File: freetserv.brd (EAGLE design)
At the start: 91.4 x 82.5 mm, 157 parts, among them IC1 MCP16311-E/MS, IC10 MAX3232ECPW, IC11 MAX3232ECPW, IC12 MAX3232ECPW, IC13 MAX3232ECPW, IC14 FT4232HL, IC15 MAX3232ECPW, IC16 MAX3232ECPW, IC17 MAX3232ECPW, IC18 MAX3232ECPW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

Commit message: wire up DAISY_OUT
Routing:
- net DX0_P: track 2.89 -> 37.9 mm
- net DX0_N: track 2.89 -> 37.8 mm
- net +5V: track 98.0 -> 103.0 mm, vias 0 -> 1
- net D1_N: track 30.1 -> 32.3 mm
- net D1_P: track 30.5 -> 32.2 mm
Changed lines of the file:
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@@
 <contactref element="K1" pad="1"/>
 <contactref element="DAISY_OUT" pad="1"/>
-<wire x1="14.859" y1="81.026" x2="81.407" y2="81.026" width="0.4064" layer="16"/>
+<wire x1="14.859" y1="81.026" x2="16.891" y2="81.026" width="0.4064" layer="16"/>
+<wire x1="16.891" y1="81.026" x2="81.407" y2="81.026" width="0.4064" layer="16"/>
 <wire x1="81.407" y1="81.026" x2="81.407" y2="72.771" width="0.4064" layer="16"/>
 <wire x1="14.859" y1="81.026" x2="10.668" y2="81.026" width="0.4064" layer="1"/>
@@
 <wire x1="9.525" y1="79.883" x2="9.525" y2="76.962" width="0.4064" layer="1"/>
 <wire x1="9.525" y1="76.962" x2="5.207" y2="72.644" width="0.4064" layer="1"/>
-<wire x1="9.525" y1="76.962" x2="9.525" y2="75.057" width="0.4064" layer="1"/>
-<wire x1="9.525" y1="75.057" x2="13.208" y2="71.374" width="0.4064" layer="1"/>
-<wire x1="13.208" y1="71.374" x2="14.419" y2="71.374" width="0.4064" layer="1"/>
 <wire x1="14.419" y1="71.374" x2="14.46" y2="71.415" width="0.4064" layer="1"/>
+<wire x1="14.419" y1="71.374" x2="13.462" y2="71.374" width="0.4064" layer="1"/>
+<wire x1="13.462" y1="71.374" x2="13.208" y2="71.628" width="0.4064" layer="1"/>
+<via x="13.208" y="71.628" extent="1-16" drill="0.3048"/>
+<wire x1="13.208" y1="71.628" x2="13.208" y2="74.041" width="0.4064" layer="16"/>
+<wire x1="13.208" y1="74.041" x2="13.716" y2="74.549" width="0.4064" layer="16"/>
+<wire x1="13.716" y1="74.549" x2="15.494" y2="74.549" width="0.4064" layer="16"/>
+<wire x1="15.494" y1="74.549" x2="16.891" y2="75.946" width="0.4064" layer="16"/>
+<wire x1="16.891" y1="75.946" x2="16.891" y2="81.026" width="0.4064" layer="16"/>
+<wire x1="14.46" y1="71.415" x2="14.46" y2="72.065" width="0" layer="19" extent="1-1"/>
+<wire x1="14.544" y1="69.215" x2="14.419" y2="71.374" width="0" layer="19" extent="1-1"/>
+<wire x1="14.544" y1="67.056" x2="14.544" y2="69.215" width="0" layer="19" extent="1-1"/>
 </signal>
 <signal name="N$3">
@@
 <wire x1="70.8725" y1="74.3712" x2="71.1225" y2="74.1212" width="0.1778" layer="1" curve="-90"/>
 <wire x1="71.1225" y1="74.1212" x2="71.1225" y2="73.503" width="0.1778" layer="1"/>
-<wire x1="71.1225" y1="73.503" x2="75.239" y2="69.3865" width="0.1778" layer="1" curve="90"/>
-<wire x1="75.239" y1="69.3865" x2="76.289" y2="69.3865" width="0.1778" layer="1"/>
+<wire x1="76.289" y1="69.3865" x2="71.5835" y2="69.3865" width="0.1778" layer="1"/>
+<wire x1="71.5835" y1="69.3865" x2="71.12" y2="69.85" width="0.1778" layer="1" curve="-90"/>
+<wire x1="71.12" y1="69.85" x2="71.12" y2="73.5005" width="0.1778" layer="1"/>
+<wire x1="71.12" y1="73.5005" x2="71.1225" y2="73.503" width="0.1778" layer="1" curve="-90"/>
 </signal>
 <signal name="D1_P" class="1">
@@
 <wire x1="51.094053125" y1="72.3138" x2="52.08856875" y2="72.3138" width="0.1778" layer="1"/>
 <wire x1="53.467" y1="72.3138" x2="66.370796875" y2="72.3138" width="0.1778" layer="1"/>
-<wire x1="76.289" y1="70.1865" x2="73.0225" y2="73.453" width="0.1778" layer="1" curve="-90"/>
-<wire x1="73.0225" y1="73.453" x2="73.0225" y2="73.503" width="0.1778" layer="1"/>
+<wire x1="73.0225" y1="70.6145" x2="73.0225" y2="73.503" width="0.1778" layer="1"/>
+<wire x1="73.0225" y1="70.6145" x2="73.279" y2="70.358" width="0.1778" layer="1" curve="90"/>
+<wire x1="73.279" y1="70.358" x2="76.1175" y2="70.358" width="0.1778" layer="1"/>
+<wire x1="76.1175" y1="70.358" x2="76.289" y2="70.1865" width="0.1778" layer="1" curve="-90"/>
 </signal>
 <signal name="DX0_N" class="1">
@@
 <wire x1="30.5625" y1="76.012290625" x2="30.5625" y2="75.603" width="0.1778" layer="1"/>
 <contactref element="DAISY_OUT" pad="3"/>
-<wire x1="5.207" y1="67.564" x2="30.5625" y2="75.603" width="0" layer="19" extent="1-1"/>
+<wire x1="30.5625" y1="75.603" x2="30.5625" y2="75.3935" width="0.1778" layer="1"/>
+<wire x1="30.5625" y1="75.3935" x2="30.226" y2="75.057" width="0.1778" layer="1" curve="-90"/>
+<wire x1="30.226" y1="75.057" x2="12.446" y2="75.057" width="0.1778" layer="1"/>
+<wire x1="12.446" y1="75.057" x2="11.938" y2="74.549" width="0.1778" layer="1" curve="90"/>
+<wire x1="11.938" y1="74.549" x2="11.938" y2="67.945" width="0.1778" layer="1"/>
+<wire x1="11.938" y1="67.945" x2="11.557" y2="67.564" width="0.1778" layer="1" curve="-90"/>
+<wire x1="11.557" y1="67.564" x2="10.730065625" y2="67.564" width="0.1778" layer="1"/>
+<wire x1="10.730065625" y1="67.564" x2="10.418915625" y2="67.87515" width="0.1778" layer="1" curve="-90"/>
+<wire x1="10.418915625" y1="67.87515" x2="10.107765625" y2="68.1863" width="0.1778" layer="1" curve="90"/>
+<wire x1="10.107765625" y1="68.1863" x2="9.985478125" y2="68.1863" width="0.1778" layer="1"/>
+<wire x1="9.985478125" y1="68.1863" x2="9.674328125" y2="67.87515" width="0.1778" layer="1" curve="90"/>
+<wire x1="9.674328125" y1="67.87515" x2="9.674328125" y2="67.25285" width="0.1778" layer="1"/>
+<wire x1="9.674328125" y1="67.25285" x2="9.363178125" y2="66.9417" width="0.1778" layer="1" curve="-90"/>
+<wire x1="9.363178125" y1="66.9417" x2="9.2408875" y2="66.9417" width="0.1778" layer="1"/>
+<wire x1="9.2408875" y1="66.9417" x2="8.9297375" y2="67.25285" width="0.1778" layer="1" curve="-90"/>
+<wire x1="8.9297375" y1="67.25285" x2="8.9297375" y2="67.87515" width="0.1778" layer="1"/>
+<wire x1="8.9297375" y1="67.87515" x2="8.6185875" y2="68.1863" width="0.1778" layer="1" curve="90"/>
+<wire x1="8.6185875" y1="68.1863" x2="8.4963" y2="68.1863" width="0.1778" layer="1"/>
+<wire x1="8.4963" y1="68.1863" x2="8.18515" y2="67.87515" width="0.1778" layer="1" curve="90"/>
+<wire x1="8.18515" y1="67.87515" x2="7.874" y2="67.564" width="0.1778" layer="1" curve="-90"/>
+<wire x1="7.874" y1="67.564" x2="5.207" y2="67.564" width="0.1778" layer="1"/>
 </signal>
 <signal name="DX0_P" class="1">
@@
 <wire x1="29.7625" y1="76.012290625" x2="29.7625" y2="75.603" width="0.1778" layer="1"/>
 <contactref element="DAISY_OUT" pad="2"/>
-<wire x1="5.207" y1="70.104" x2="29.7625" y2="75.603" width="0" layer="19" extent="1-1"/>
+<wire x1="12.357" y1="75.603" x2="29.7625" y2="75.603" width="0.1778" layer="1"/>
+<wire x1="12.357" y1="75.603" x2="11.43" y2="74.676" width="0.1778" layer="1" curve="90"/>
+<wire x1="11.43" y1="74.676" x2="11.43" y2="70.612" width="0.1778" layer="1"/>
+<wire x1="11.43" y1="70.612" x2="10.922" y2="70.104" width="0.1778" layer="1" curve="-90"/>
+<wire x1="10.922" y1="70.104" x2="10.914053125" y2="70.104" width="0.1778" layer="1"/>
+<wire x1="10.914053125" y1="70.104" x2="10.602903125" y2="69.79285" width="0.1778" layer="1" curve="90"/>
+<wire x1="10.602903125" y1="69.79285" x2="10.602903125" y2="69.620953125" width="0.1778" layer="1"/>
+<wire x1="10.602903125" y1="69.620953125" x2="10.291753125" y2="69.309803125" width="0.1778" layer="1" curve="-90"/>
+<wire x1="10.291753125" y1="69.309803125" x2="10.278103125" y2="69.309803125" width="0.1778" layer="1"/>
+<wire x1="10.278103125" y1="69.309803125" x2="9.966953125" y2="69.620953125" width="0.1778" layer="1" curve="-90"/>
+<wire x1="9.966953125" y1="69.620953125" x2="9.966953125" y2="70.587046875" width="0.1778" layer="1"/>
+<wire x1="9.966953125" y1="70.587046875" x2="9.655803125" y2="70.898196875" width="0.1778" layer="1" curve="90"/>
+<wire x1="9.655803125" y1="70.898196875" x2="9.642153125" y2="70.898196875" width="0.1778" layer="1"/>
+<wire x1="9.642153125" y1="70.898196875" x2="9.331003125" y2="70.587046875" width="0.1778" layer="1" curve="90"/>
+<wire x1="9.331003125" y1="70.587046875" x2="9.331003125" y2="69.620953125" width="0.1778" layer="1"/>
+<wire x1="9.331003125" y1="69.620953125" x2="9.019853125" y2="69.309803125" width="0.1778" layer="1" curve="-90"/>
+<wire x1="9.019853125" y1="69.309803125" x2="9.0062" y2="69.309803125" width="0.1778" layer="1"/>
+<wire x1="9.0062" y1="69.309803125" x2="8.69505" y2="69.620953125" width="0.1778" layer="1" curve="-90"/>
+<wire x1="8.69505" y1="69.620953125" x2="8.69505" y2="70.587046875" width="0.1778" layer="1"/>
+<wire x1="8.69505" y1="70.587046875" x2="8.3839" y2="70.898196875" width="0.1778" layer="1" curve="90"/>
+<wire x1="8.3839" y1="70.898196875" x2="8.37025" y2="70.898196875" width="0.1778" layer="1"/>
+<wire x1="8.37025" y1="70.898196875" x2="8.0591" y2="70.587046875" width="0.1778" layer="1" curve="90"/>
+<wire x1="8.0591" y1="70.587046875" x2="8.0591" y2="69.620953125" width="0.1778" layer="1"/>
+<wire x1="8.0591" y1="69.620953125" x2="7.74795" y2="69.309803125" width="0.1778" layer="1" curve="-90"/>
+<wire x1="7.74795" y1="69.309803125" x2="7.7343" y2="69.309803125" width="0.1778" layer="1"/>
+<wire x1="7.7343" y1="69.309803125" x2="7.42315" y2="69.620953125" width="0.1778" layer="1" curve="-90"/>
+<wire x1="7.42315" y1="69.620953125" x2="7.42315" y2="69.79285" width="0.1778" layer="1"/>
+<wire x1="7.42315" y1="69.79285" x2="7.112" y2="70.104" width="0.1778" layer="1" curve="90"/>
+<wire x1="7.112" y1="70.104" x2="5.207" y2="70.104" width="0.1778" layer="1"/>
 </signal>
 <signal name="D0_N" class="1">

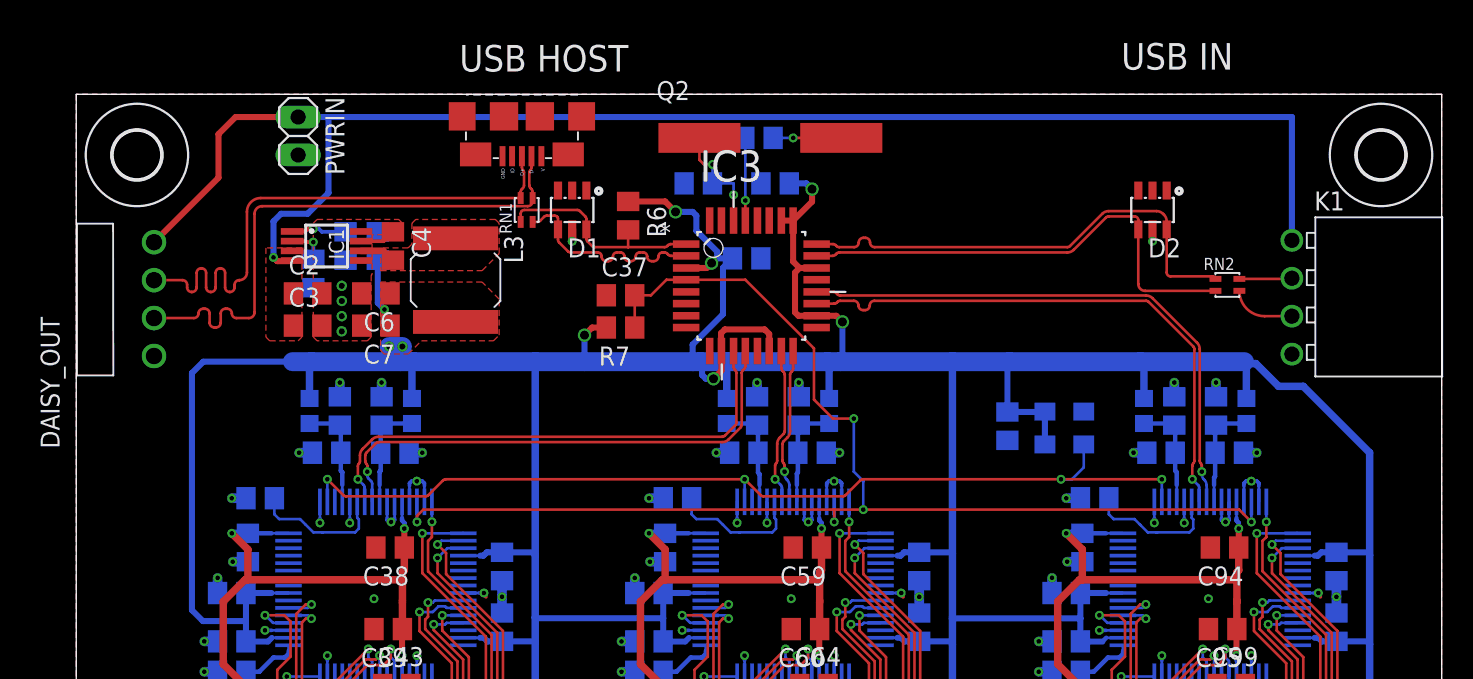
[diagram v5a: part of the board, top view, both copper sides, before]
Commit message: add tPlace documentation (port descriptions, version)
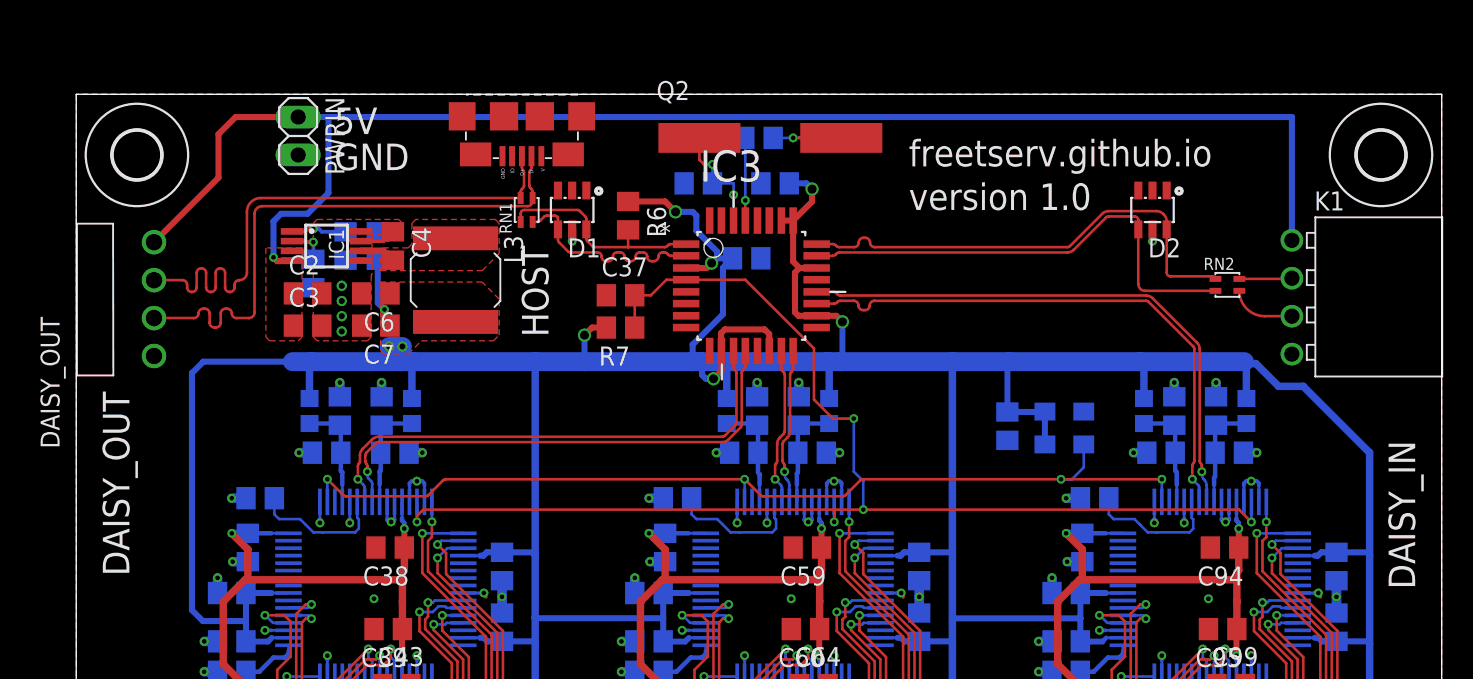
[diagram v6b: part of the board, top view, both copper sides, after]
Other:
- board text added: "5V"
- board text added: "DAISY_IN"
- board text added: "DAISY_OUT"
- board text added: "GND"
- board text added: "HOST"
- board text added: "freetserv.github.io"
- board text added: "version 1.0"
- board text removed: "USB HOST"
- board text removed: "USB IN"
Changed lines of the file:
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@@
 <wire x1="91.44" y1="82.55" x2="0" y2="82.55" width="0" layer="20"/>
 <wire x1="0" y1="82.55" x2="0" y2="0" width="0" layer="20"/>
-<text x="69.977" y="84.201" size="1.778" layer="21">USB IN</text>
-<text x="25.654" y="84.074" size="1.778" layer="21">USB HOST</text>
+<text x="31.623" y="66.294" size="1.778" layer="21" rot="R90">HOST</text>
+<text x="17.272" y="77.47" size="1.778" layer="21">GND</text>
+<text x="17.272" y="79.883" size="1.778" layer="21">5V</text>
+<text x="3.556" y="50.292" size="1.778" layer="21" rot="R90">DAISY_OUT</text>
+<text x="89.662" y="49.403" size="1.778" layer="21" rot="R90">DAISY_IN</text>
+<text x="55.753" y="77.724" size="1.778" layer="21">freetserv.github.io</text>
+<text x="55.753" y="74.803" size="1.778" layer="21">version 1.0</text>
 </plain>
 <attributes>
@@
 <wire x1="15.494" y1="74.549" x2="16.891" y2="75.946" width="0.4064" layer="16"/>
 <wire x1="16.891" y1="75.946" x2="16.891" y2="81.026" width="0.4064" layer="16"/>
-<wire x1="14.46" y1="71.415" x2="14.46" y2="72.065" width="0" layer="19" extent="1-1"/>
-<wire x1="14.544" y1="69.215" x2="14.419" y2="71.374" width="0" layer="19" extent="1-1"/>
-<wire x1="14.544" y1="67.056" x2="14.544" y2="69.215" width="0" layer="19" extent="1-1"/>
 </signal>
 <signal name="N$3">

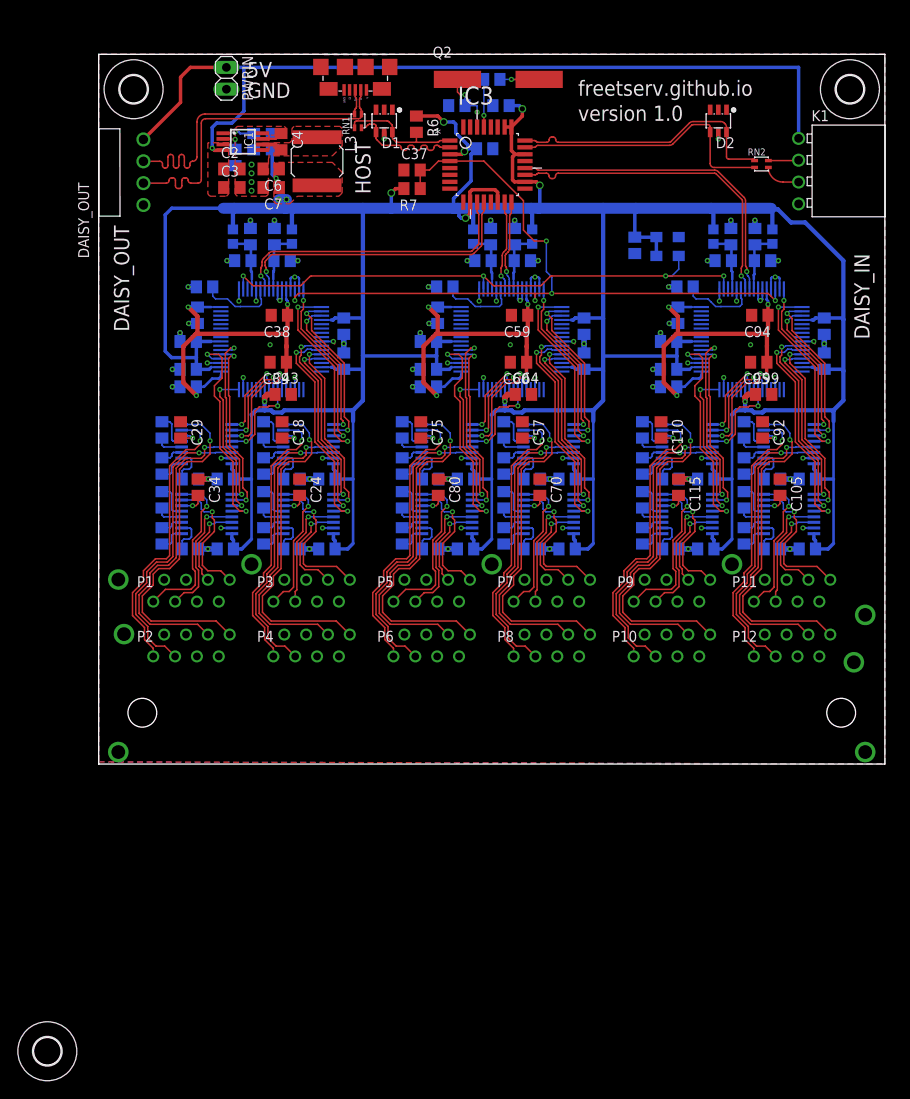
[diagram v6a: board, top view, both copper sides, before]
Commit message: re-route DAISY_OUT’s USB traces
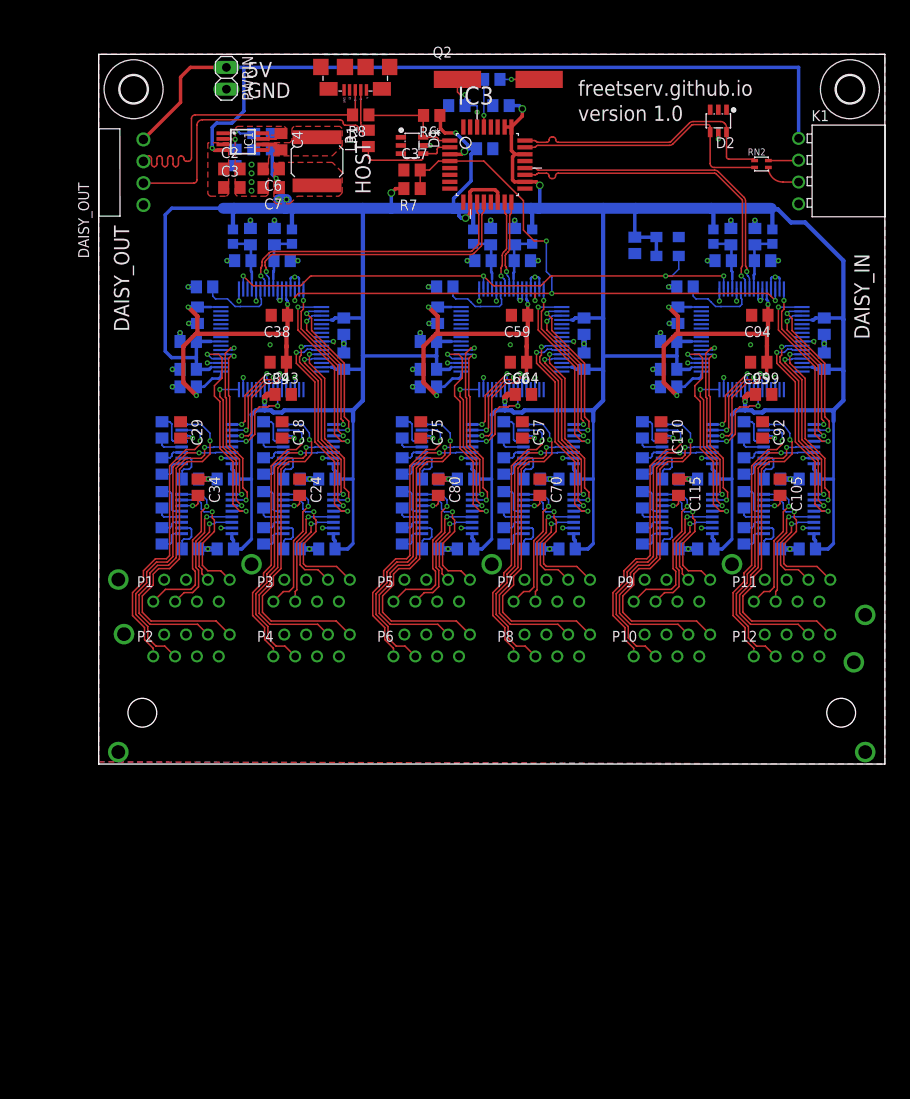
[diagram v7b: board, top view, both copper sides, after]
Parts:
- removed H4: MOUNT-HOLE3.2, holes:3,2
- removed RN1: 27, resistor-net:EXBV4V
- added R1, R8: 27, resistor:R0805
- moved D1 4.32 mm to (36.4, 71.9), turned to 270 degrees
- moved R6 2.05 mm to (38.7, 75.4), turned to 180 degrees
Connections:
- net D0_N: now also R1.1; no longer RN1.B1
- net D0_P: now also R8.1; no longer RN1.A1
- net DX0_N: now also R1.2; no longer RN1.B2
- net DX0_P: now also R8.2; no longer RN1.A2
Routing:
- net D0_P: track 14.8 -> 12.2 mm
- net +3V3: track 513.0 -> 510.8 mm
- net D0_N: track 13.9 -> 12.0 mm
- net DX0_N: track 37.8 -> 38.7 mm
